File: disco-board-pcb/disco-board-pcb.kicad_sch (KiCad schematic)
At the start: 6 parts, among them J101 Conn_02x32_Odd_Even, J102 Conn_02x32_Odd_Even, U101 MMA8653FCR1

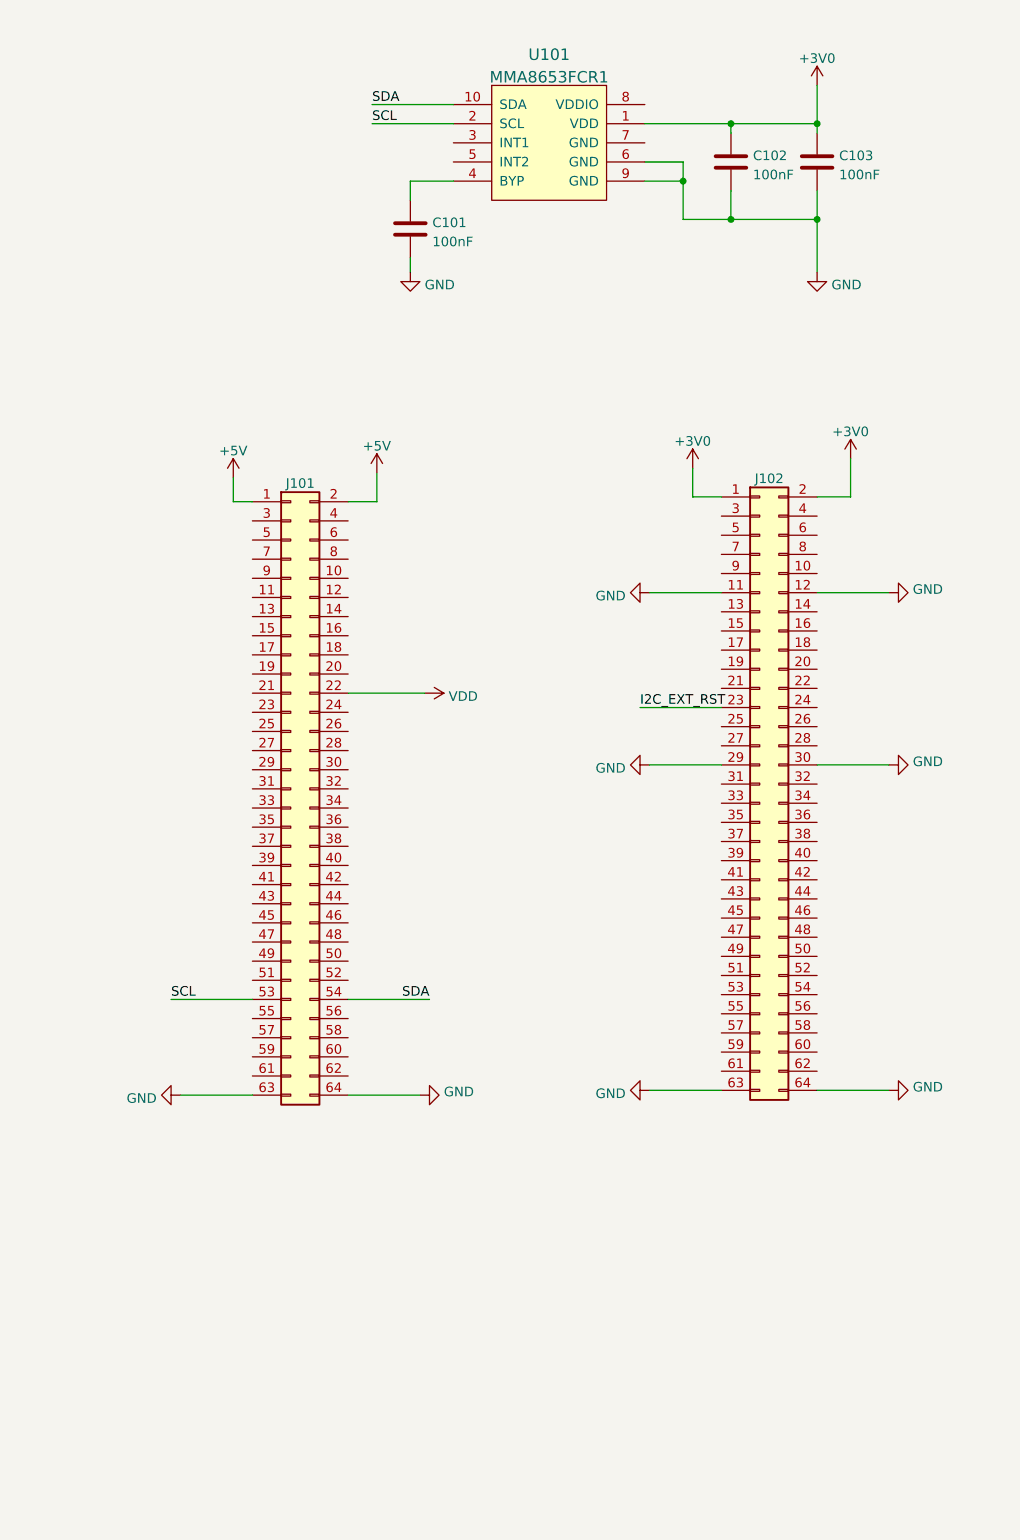
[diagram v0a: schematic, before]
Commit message: Completing schematic and putting test points on PCB
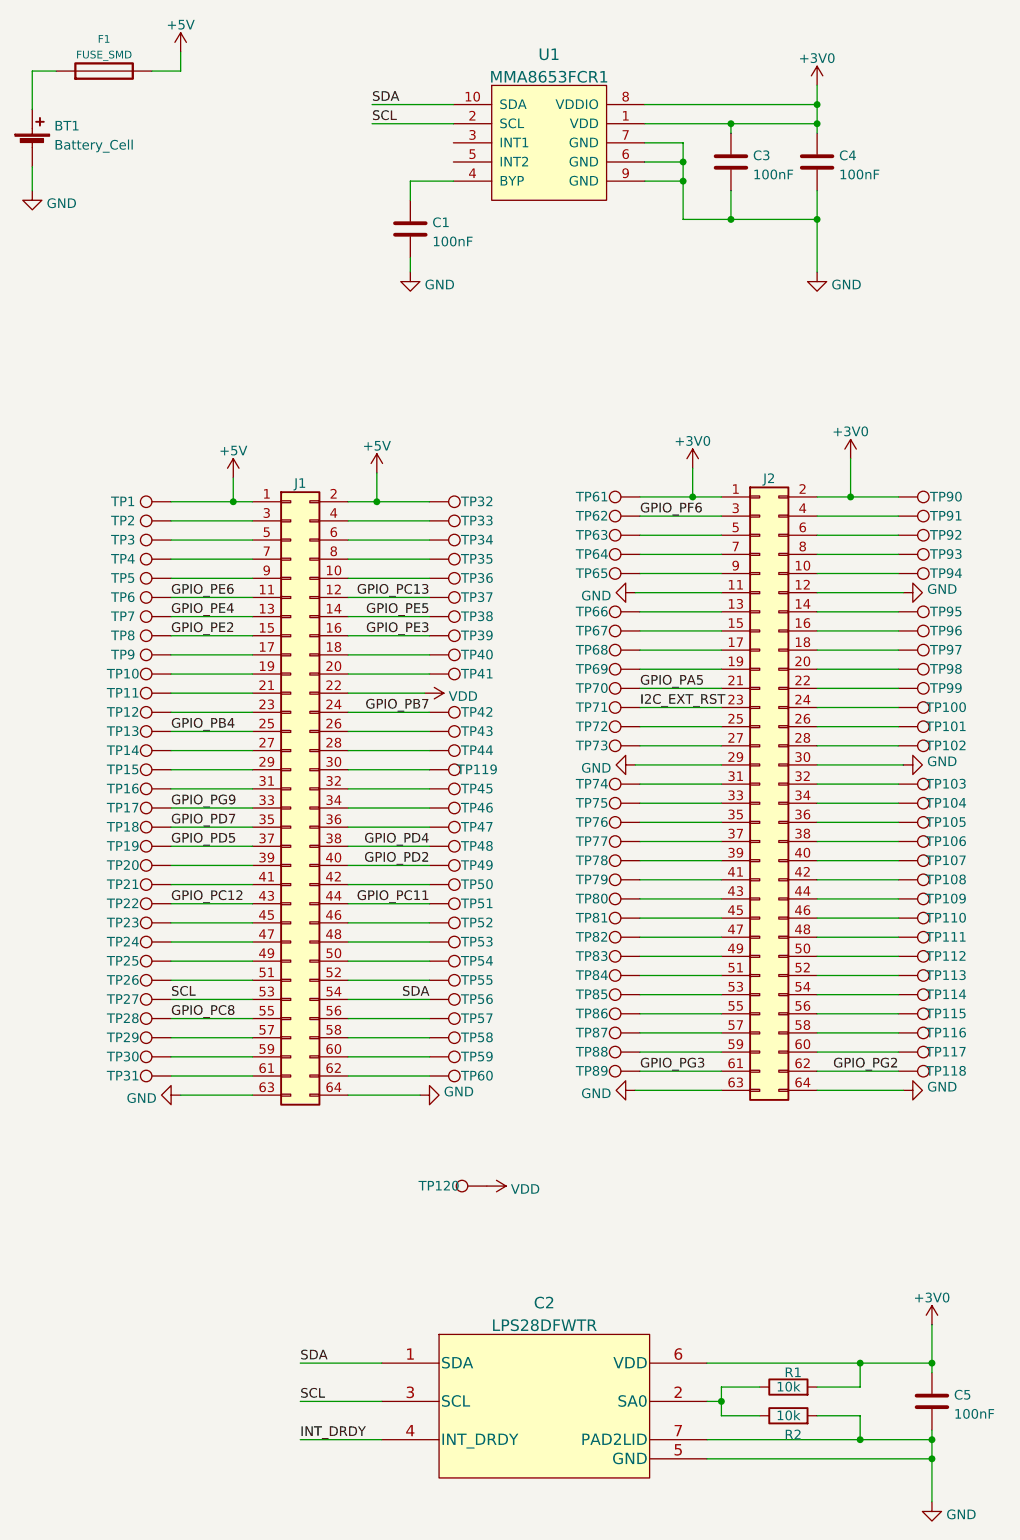
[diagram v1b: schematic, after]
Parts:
- added BT1: Battery_Cell, Battery:BatteryHolder_MPD_BH-18650-PC2, symbol Device:Battery_Cell
- added C2: LPS28DFWTR, local:LPS28DFWTR, symbol LPS28DFW:LPS28DFWTR
- added C5: 100nF, Capacitor_SMD_AKL:C_0603_1608Metric_Pad1.05x0.95mm, symbol Device:C
- added F1: FUSE_SMD, Fuse_AKL:Fuse_1206_3216Metric_Pad1.42x1.75mm_BigPads, symbol Special-local:FUSE_SMD
- added R1, R2: 10k, Resistor_SMD_AKL:R_0603_1608Metric_Pad1.05x0.95mm, symbol Device:R
- added TP1, TP10, TP100, TP101, TP102, TP103, TP104, TP105, TP106, TP107, TP108, TP109, TP11, TP110, TP111, TP112, TP113, TP114, TP115, TP116, TP117, TP118, TP119, TP12, TP120, TP13, TP14, TP15, TP16, TP17, TP18, TP19, TP2, TP20, TP21, TP22, TP23, TP24, TP25, TP26, TP27, TP28, TP29, TP3, TP30, TP31, TP32, TP33, TP34, TP35, TP36, TP37, TP38, TP39, TP4, TP40, TP41, TP42, TP43, TP44, TP45, TP46, TP47, TP48, TP49, TP5, TP50, TP51, TP52, TP53, TP54, TP55, TP56, TP57, TP58, TP59, TP6, TP60, TP61, TP62, TP63, TP64, TP65, TP66, TP67, TP68, TP69, TP7, TP70, TP71, TP72, TP73, TP74, TP75, TP76, TP77, TP78, TP79, TP8, TP80, TP81, TP82, TP83, TP84, TP85, TP86, TP87, TP88, TP89, TP9, TP90, TP91, TP92, TP93, TP94, TP95, TP96, TP97, TP98, TP99: TestPoint, TestPoint:TestPoint_Pad_D1.5mm, symbol Connector:TestPoint
- renumbered C101 to C1, C102 to C3, C103 to C4, J101 to J1, J102 to J2, U101 to U1
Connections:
- net +3V0: now also U1.8 (VDDIO), C2.6 (VDD), C5.1, R1.2, TP61.1, TP90.1
- net +5V: now also F1.2, TP1.1, TP32.1
- net GND: now also U1.7 (GND), BT1.2 (-), C2.5 (GND), C2.7 (PAD2LID), C5.2, R2.2
- net I2C_EXT_RST: now also TP71.1
- net SCL: now also C2.3 (SCL), TP27.1
- net SDA: now also C2.1 (SDA), TP56.1
- net VDD: now also TP120.1
- net at J1.10 (Pin_10): now also TP36.1
- net GPIO_PE6: now reaches J1.11 (Pin_11)
- net GPIO_PE6: now also TP6.1
- net GPIO_PC13: now reaches J1.12 (Pin_12)
- net GPIO_PC13: now also TP37.1
- net GPIO_PE4: now reaches J1.13 (Pin_13)
- net GPIO_PE4: now also TP7.1
- net GPIO_PE5: now reaches J1.14 (Pin_14)
- net GPIO_PE5: now also TP38.1
- net GPIO_PE2: now reaches J1.15 (Pin_15)
- net GPIO_PE2: now also TP8.1
- net GPIO_PE3: now reaches J1.16 (Pin_16)
- net GPIO_PE3: now also TP39.1
- net at J1.17 (Pin_17): now also TP9.1
- net at J1.18 (Pin_18): now also TP40.1
- net at J1.19 (Pin_19): now also TP10.1
- net at J1.20 (Pin_20): now also TP41.1
- net at J1.21 (Pin_21): now also TP11.1
- net at J1.23 (Pin_23): now also TP12.1
- net GPIO_PB7: now reaches J1.24 (Pin_24)
- net GPIO_PB7: now also TP42.1
- net GPIO_PB4: now reaches J1.25 (Pin_25)
- net GPIO_PB4: now also TP13.1
- net at J1.26 (Pin_26): now also TP43.1
- net at J1.27 (Pin_27): now also TP14.1
- net at J1.28 (Pin_28): now also TP44.1
- net at J1.29 (Pin_29): now also TP15.1
- net at J1.3 (Pin_3): now also TP2.1
- net at J1.30 (Pin_30): now also TP119.1
- net at J1.31 (Pin_31): now also TP16.1
- net at J1.32 (Pin_32): now also TP45.1
- net GPIO_PG9: now reaches J1.33 (Pin_33)
- net GPIO_PG9: now also TP17.1
- net at J1.34 (Pin_34): now also TP46.1
- net GPIO_PD7: now reaches J1.35 (Pin_35)
- net GPIO_PD7: now also TP18.1
- net at J1.36 (Pin_36): now also TP47.1
- net GPIO_PD5: now reaches J1.37 (Pin_37)
- net GPIO_PD5: now also TP19.1
- net GPIO_PD4: now reaches J1.38 (Pin_38)
- net GPIO_PD4: now also TP48.1
- net at J1.39 (Pin_39): now also TP20.1
- net at J1.4 (Pin_4): now also TP33.1
- net GPIO_PD2: now reaches J1.40 (Pin_40)
- net GPIO_PD2: now also TP49.1
- net at J1.41 (Pin_41): now also TP21.1
- net at J1.42 (Pin_42): now also TP50.1
- net GPIO_PC12: now reaches J1.43 (Pin_43)
- net GPIO_PC12: now also TP22.1
- net GPIO_PC11: now reaches J1.44 (Pin_44)
- net GPIO_PC11: now also TP51.1
- net at J1.45 (Pin_45): now also TP23.1
- net at J1.46 (Pin_46): now also TP52.1
- net at J1.47 (Pin_47): now also TP24.1
- net at J1.48 (Pin_48): now also TP53.1
- net at J1.49 (Pin_49): now also TP25.1
- net at J1.5 (Pin_5): now also TP3.1
- net at J1.50 (Pin_50): now also TP54.1
- net at J1.51 (Pin_51): now also TP26.1
- net at J1.52 (Pin_52): now also TP55.1
- net GPIO_PC8: now reaches J1.55 (Pin_55)
- net GPIO_PC8: now also TP28.1
- net at J1.56 (Pin_56): now also TP57.1
- net at J1.57 (Pin_57): now also TP29.1
- net at J1.58 (Pin_58): now also TP58.1
- net at J1.59 (Pin_59): now also TP30.1
- net at J1.6 (Pin_6): now also TP34.1
- net at J1.60 (Pin_60): now also TP59.1
- net at J1.61 (Pin_61): now also TP31.1
- net at J1.62 (Pin_62): now also TP60.1
- net at J1.7 (Pin_7): now also TP4.1
- net at J1.8 (Pin_8): now also TP35.1
- net at J1.9 (Pin_9): now also TP5.1
- net at J2.10 (Pin_10): now also TP94.1
- net at J2.13 (Pin_13): now also TP66.1
- net at J2.14 (Pin_14): now also TP95.1
- net at J2.15 (Pin_15): now also TP67.1
- net at J2.16 (Pin_16): now also TP96.1
- net at J2.17 (Pin_17): now also TP68.1
- net at J2.18 (Pin_18): now also TP97.1
- net at J2.19 (Pin_19): now also TP69.1
- net at J2.20 (Pin_20): now also TP98.1
- net GPIO_PA5: now reaches J2.21 (Pin_21)
- net GPIO_PA5: now also TP70.1
- net at J2.22 (Pin_22): now also TP99.1
- net at J2.24 (Pin_24): now also TP100.1
- net at J2.25 (Pin_25): now also TP72.1
- net at J2.26 (Pin_26): now also TP101.1
- net at J2.27 (Pin_27): now also TP73.1
- net at J2.28 (Pin_28): now also TP102.1
- net GPIO_PF6: now reaches J2.3 (Pin_3)
- net GPIO_PF6: now also TP62.1
- net at J2.31 (Pin_31): now also TP74.1
- net at J2.32 (Pin_32): now also TP103.1
- net at J2.33 (Pin_33): now also TP75.1
- net at J2.34 (Pin_34): now also TP104.1
- net at J2.35 (Pin_35): now also TP76.1
- net at J2.36 (Pin_36): now also TP105.1
- net at J2.37 (Pin_37): now also TP77.1
- net at J2.38 (Pin_38): now also TP106.1
- net at J2.39 (Pin_39): now also TP78.1
- net at J2.4 (Pin_4): now also TP91.1
- net at J2.40 (Pin_40): now also TP107.1
- net at J2.41 (Pin_41): now also TP79.1
- net at J2.42 (Pin_42): now also TP108.1
- net at J2.43 (Pin_43): now also TP80.1
- net at J2.44 (Pin_44): now also TP109.1
- net at J2.45 (Pin_45): now also TP81.1
- net at J2.46 (Pin_46): now also TP110.1
- net at J2.47 (Pin_47): now also TP82.1
- net at J2.48 (Pin_48): now also TP111.1
- net at J2.49 (Pin_49): now also TP83.1
- net at J2.5 (Pin_5): now also TP63.1
- net at J2.50 (Pin_50): now also TP112.1
- net at J2.51 (Pin_51): now also TP84.1
- net at J2.52 (Pin_52): now also TP113.1
- net at J2.53 (Pin_53): now also TP85.1
- net at J2.54 (Pin_54): now also TP114.1
- net at J2.55 (Pin_55): now also TP86.1
- net at J2.56 (Pin_56): now also TP115.1
- net at J2.57 (Pin_57): now also TP87.1
- net at J2.58 (Pin_58): now also TP116.1
- net at J2.59 (Pin_59): now also TP88.1
- net at J2.6 (Pin_6): now also TP92.1
- net at J2.60 (Pin_60): now also TP117.1
- net GPIO_PG3: now reaches J2.61 (Pin_61)
- net GPIO_PG3: now also TP89.1
- net GPIO_PG2: now reaches J2.62 (Pin_62)
- net GPIO_PG2: now also TP118.1
- net at J2.7 (Pin_7): now also TP64.1
- net at J2.8 (Pin_8): now also TP93.1
- net at J2.9 (Pin_9): now also TP65.1
- new net: C2.2 (SA0), R1.1, R2.1
- new net: BT1.1 (+), F1.1
- new net INT_DRDY: C2.4 (INT_DRDY)
